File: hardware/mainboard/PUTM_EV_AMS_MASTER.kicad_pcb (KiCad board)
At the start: 4 copper layers, 60 x 100 mm, 207 parts, among them IC1 3.3V/0.5A, IC2 TPS54202HDDCR, IC3 BQ79600PWRQ1, IC6 AMC3330DWER, IC7 AMC3330DWER, IC8 ADC 24bit, IC9 LTC1799, J1 M80-5100642, J10 M300-MV10345M1, J2 M80-5102042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

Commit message: chore: sync
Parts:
- removed C34, C44, C83, C84, C85: 100nF, Capacitor_SMD:C_0603_1608Metric
- removed D10, D13, D18, D19, D24, D8, D9: 60V/0.5/3A, Diode_SMD:D_SOD-123
- removed Q1, Q2, Q3, Q7: DMT6018LDR-7, Samacsys:DMT6018LDR7
- removed R30, R37, R44, R45, R5, R58, R59: 100, Resistor_SMD:R_0603_1608Metric
- removed R46, R47, R48, R56, R57, R60, R61, R71: 10k, Resistor_SMD:R_0603_1608Metric
- removed U2: FT230XS, Package_SO:SSOP-16_3.9x4.9mm_P0.635mm
- added C1: 22uF, Capacitor_SMD:C_0805_2012Metric, F.Cu at (51.5, 154.5)
- J1: value M80-5100642 -> Conn_02x10_Odd_Even; footprint Samacsys:M80-51006YY -> Connector_PinHeader_2.00mm:PinHeader_2x10_P2.00mm_Vertical
- J2: value M80-5102042 -> Conn_02x03_Odd_Even; footprint Samacsys:M80-51020YY -> Connector_PinHeader_2.00mm:PinHeader_2x03_P2.00mm_Vertical
- J3: value M80-5100842 -> Conn_02x04_Odd_Even; footprint Samacsys:M80-51008YY -> Connector_PinHeader_2.00mm:PinHeader_2x04_P2.00mm_Vertical
- moved D16 75.6 mm to (74.4, 144.2)
- moved D5 75.6 mm to (74.4, 144.2)
- moved C11 75.6 mm to (56.2, 142.1)
- moved C12 75.6 mm to (59.7, 140.1)
- moved C13 75.6 mm to (44.9, 130.6)
- moved C14 75.6 mm to (44.9, 129.1)
- moved C17 75.6 mm to (59.7, 138.1)
- moved C19 75.6 mm to (69.4, 97.6)
- moved C20 75.6 mm to (69.4, 95.6)
- moved C21 75.6 mm to (59.7, 142.1)
- moved C22 75.6 mm to (56.2, 138.1)
- moved C23 75.6 mm to (51.9, 118.1)
- moved C24 75.6 mm to (63.4, 111.1)
- moved C25 75.6 mm to (61.2, 120.4)
- moved C26 75.6 mm to (56.2, 140.1)
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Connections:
- net Net-(IC8-CH0+) renamed /ADC/+5VA_MEAS
- D11 pad 1: /EX_CANFD2_TX -> /CTX2
- D11 pad 2: /EX_CANFD2_RX -> /CRX2
- D12 pad 1: /D+ -> /UTX
- D12 pad 2: /D- -> /URX
- D4 pad 1: /EX_CANFD1_TX -> /CTX1
- D4 pad 2: /EX_CANFD1_RX -> /CRX1
- J1 pad 1: /AIR_M- -> /D-
- J1 pad 2: /AIR_P- -> GND
- J1 pad 3: /AIR_PRE- -> /D+
- J1 pad 4: +24V -> VBUS+
- J1 pad 5: +24V -> /EX_CANFD1_RX
- J1 pad 6: +24V -> /CHARGER_DETECTION
- J2 pad 1: /D- -> /AIR_M-
- J2 pad 2: /D+ -> unconnected-(J2-Pin_2-Pad2)
- J2 pad 3: /EX_CANFD1_RX -> /AIR_P-
- J2 pad 4: /EX_CANFD1_TX -> unconnected-(J2-Pin_4-Pad4)
- J2 pad 5: /EX_CANFD2_RX -> /AIR_PRE-
- J2 pad 6: /EX_CANFD2_TX -> unconnected-(J2-Pin_6-Pad6)
- J3 pad 2: /FAN2- -> unconnected-(J3-Pin_2-Pad2)
- J3 pad 3: /FAN3- -> /FAN2-
- J3 pad 4: /FAN4- -> unconnected-(J3-Pin_4-Pad4)
- J3 pad 5: +24V -> /FAN3-
- J3 pad 6: +24V -> unconnected-(J3-Pin_6-Pad6)
- J3 pad 7: +24V -> /FAN4-
- J3 pad 8: +24V -> unconnected-(J3-Pin_8-Pad8)
- R7 pad 1: /D+ -> /Connectivity/EX_FTDI_D+
- R7 pad 2: /Connectivity/FTDIU+ -> /UTX
- R8 pad 1: /Connectivity/FTDIU- -> /URX
- R8 pad 2: /D- -> /Connectivity/EX_FTDI_D-
- U10 pad 2: /Connectivity/~{FTDI_RST} -> /MCU/~{FTDI_RST}
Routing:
- net GND: track 144.5 -> 13.5 mm, vias 103 -> 7
- net (no net): track 88.8 -> 0.00 mm
- net +24V: track 74.5 -> 0.00 mm, vias 7 -> 0
- net VBUS+: track 67.7 -> 0.00 mm, vias 2 -> 0
- net /AIR_PRE_DETECTION: track 63.7 -> 0.00 mm, vias 3 -> 0
- net /AIR_P_DETECTION: track 59.5 -> 0.00 mm, vias 3 -> 0
- net /AIR_M_DETECTION: track 58.8 -> 0.00 mm, vias 1 -> 0
- net /CHARGER_DETECTION: track 56.3 -> 0.00 mm, vias 1 -> 0
- net /SWCLK: track 56.0 -> 0.00 mm, vias 2 -> 0
- net /SWDIO: track 48.3 -> 0.00 mm, vias 2 -> 0
- net /AMS_ERROR: track 46.3 -> 0.00 mm, vias 3 -> 0
- net /UART_TX: track 45.7 -> 0.00 mm, vias 2 -> 0
- net /DETVUSB: track 44.7 -> 0.00 mm, vias 2 -> 0
- net /FC1: track 44.1 -> 0.00 mm, vias 1 -> 0
- net /UART_RX: track 42.7 -> 0.00 mm, vias 2 -> 0
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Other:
- board text removed: "IN"
- board text removed: "OUT"

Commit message: jenrzej colab
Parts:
- moved J8 5.70 mm to (158.5, 83.3)
- moved J4 3.57 mm to (105.5, 91.4)
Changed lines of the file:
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@@
 	(footprint "Samacsys:FTSH-107-XX-YYY-D-K"
 		(layer "F.Cu")
-		(at 105.5 95 90)
+		(at 105.5 91.43 90)
 		(descr "FTSH-107-XX-YYY-D-K")
 		(tags "Connector")
@@
 	(footprint "Samacsys:M80-51004YY"
 		(layer "F.Cu")
-		(at 158.5 89 -90)
+		(at 158.5 83.3 -90)
 		(descr "M80-51004YY")
 		(tags "Connector")

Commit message: Cleaned up schematic, changed USB to UART, changed pinout of AIR sandwich connector
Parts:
- removed C1, C11, C12, C17, C26, C68: 22uF, Capacitor_SMD:C_0805_2012Metric
- removed C13, C14, C3: 1uF, Capacitor_SMD:C_0603_1608Metric
- removed C19, C20, C4, C5: 2.2uF, Capacitor_SMD:C_0603_1608Metric
- removed C21, C22, C39, C40, C42, C56, C57: 100nF, Capacitor_SMD:C_0603_1608Metric
- removed C27, C6, C65: 22uF, Capacitor_SMD:CP_Elec_4x5.8
- removed D12: 5.3V/400W, Package_TO_SOT_SMD:SOT-23-3
- removed D14: 6V, Diode_SMD:D_SOD-123
- removed D16: 30V, Diode_SMD:D_SOD-123
- removed F2: 5A/24V, Fuse:Fuse_2920_7451Metric
- removed F4, F5, F8: 5V/0.5A, Fuse:Fuse_0805_2012Metric
- removed FB1, FB2: 100@100Mhz, Inductor_SMD:L_0603_1608Metric
- removed the H3 at (158.5, 144.5)
- removed IC1: 3.3V/0.5A, Package_TO_SOT_SMD:SOT-23-5
- removed IC2: TPS54202HDDCR, Package_TO_SOT_SMD:SOT-23-6
- removed L4: 68uF/1.4A, Inductor_SMD:L_TDK_VLS6045EX_VLS6045AF
- removed Q4: SI2347DS-T1-GE3, Package_TO_SOT_SMD:SOT-23-3
- removed R10: 100k, Resistor_SMD:R_0603_1608Metric_Pad0.98x0.95mm_HandSolder
- removed R16: 20k, Resistor_SMD:R_0603_1608Metric
- removed R23: 510k, Resistor_SMD:R_0603_1608Metric
- removed R28, R35, R39: 100k, Resistor_SMD:R_0603_1608Metric
- removed R29: 13.3k, Resistor_SMD:R_0603_1608Metric
- removed R32: 10k, Resistor_SMD:R_0603_1608Metric
- removed R40: 400, Resistor_SMD:R_0603_1608Metric
- removed R7, R8: 27, Resistor_SMD:R_0603_1608Metric
- removed TP3, TP9: TestPoint_Small, TestPoint:TestPoint_THTPad_D1.0mm_Drill0.5mm
- removed U4: TPS2113PWR, Package_SO:TSSOP-8_4.4x3mm_P0.65mm
- added H1: M3, MountingHole:MountingHole_3.2mm_M3, F.Cu at (158.5, 86.5)
- D5: value 10V -> ESDS304; footprint Diode_SMD:D_SOD-123 -> Package_TO_SOT_SMD:SOT-23-5_HandSoldering
- moved R73 123.4 mm to (66.4, 92.5)
- moved C96 123.1 mm to (66.4, 91.0)
- moved R72 120.3 mm to (69.3, 91.0)
- moved D5 111.4 mm to (182.6, 117.5)
- moved C23 85.8 mm to (137.6, 121.3)
- moved C29 83.3 mm to (135.6, 132.4), turned to 180 degrees
- moved C28 83.3 mm to (134.7, 121.3)
- moved C36 78.5 mm to (135.4, 124.5), turned to -90 degrees
- moved C70 78.2 mm to (137.4, 124.5), turned to -90 degrees
- moved U10 76.9 mm to (133.6, 126.7), turned to 90 degrees
- moved C25 75.0 mm to (136.1, 121.3), turned to 90 degrees
- moved C86 73.9 mm to (127.9, 112.6), turned to 180 degrees
- moved C24 71.5 mm to (133.7, 124.3)
- moved D27 70.9 mm to (110.1, 134.5)
- moved C87 70.9 mm to (130.3, 130.0), turned to 0 degrees
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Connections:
- D5 pad 1: +24V -> /UART_RX
- D5 pad 2: Net-(D5-A) -> GND
- J1 pad 1: /D- -> /UART_TX
- J1 pad 10: /AIR_PRE_DETECTION -> unconnected-(J1-Pin_10-Pad10)
- J1 pad 12: /AIR_M_DETECTION -> unconnected-(J1-Pin_12-Pad12)
- J1 pad 15: unconnected-(J1-Pin_15-Pad15) -> +5VA
- J1 pad 19: VDD -> +3.3VA
- J1 pad 3: /D+ -> /UART_RX
- J1 pad 4: VBUS+ -> /DETVUSB
- J1 pad 6: /CHARGER_DETECTION -> /UART_RST
- J1 pad 8: /AIR_P_DETECTION -> unconnected-(J1-Pin_8-Pad8)
- U10 pad 14: /FC1 -> /FAN1-
- U10 pad 15: /FC2 -> /FAN2-
- U10 pad 16: /FC3 -> /FAN3-
- U10 pad 17: /FC4 -> /FAN4-
- U10 pad 2: /MCU/~{FTDI_RST} -> /UART_RST
- U10 pad 33: /SAE -> /AIR_PRE-
- U10 pad 34: /SAP -> /AIR_P-
- U10 pad 35: /SAM -> /AIR_M-
- U10 pad 42: /UTX -> /UART_RX
- U10 pad 43: /URX -> /UART_TX
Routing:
- net /ADC/ACU_V-: track 12.6 -> 0.00 mm
- net /Safety/LATCHERR: track 0.00 -> 9.71 mm, vias 0 -> 1
- net +5VIO: track 9.08 -> 18.5 mm, vias 2 -> 4
- net /CRX2: track 0.00 -> 8.41 mm
- net Net-(R14-Pad2): track 0.00 -> 7.63 mm, vias 0 -> 1
- net /CTX2: track 0.00 -> 7.51 mm
- net /Safety/CT_G: track 0.00 -> 7.37 mm, vias 0 -> 1
- net /CRX1: track 0.00 -> 7.06 mm
- net /CTX1: track 0.00 -> 7.02 mm
- net /AMS_ERROR: track 0.00 -> 4.94 mm, vias 0 -> 1
- net /Safety/CAP_VOLT: track 0.00 -> 4.28 mm, vias 0 -> 1
- net /CAR_I: track 0.00 -> 4.20 mm
- net /Isolated SPI/OUT+: track 3.75 -> 0.00 mm
- net /Isolated SPI/OUT-: track 3.71 -> 0.00 mm
- net /ADC/+5VA_MEAS: track 0.00 -> 2.87 mm
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- added copper zone on B.Cu, net GND
- added copper zone on F.Cu, net GND
- added copper zone on In2.Cu, net GND
- removed copper zone on In2.Cu, net +24V
- removed copper zone on In2.Cu, net +3.3VA
- removed copper zone on In2.Cu, net +3.3VIO
- removed copper zone on In2.Cu, net +3.3VMCU
- removed copper zone on In2.Cu, net +5VA
- removed copper zone on In2.Cu, net +5VIO
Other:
- board text added: "UART"
- board text removed: "24V"
- board text removed: "3.3V"
- board text removed: "5V"
- board text removed: "AIR CR"
- board text removed: "ANALOG PWR"
- board text removed: "FAN CR"
- board text removed: "LEDS"
- board text removed: "MUX5V"
- board text removed: "USB"
- board text removed: "USB5V"

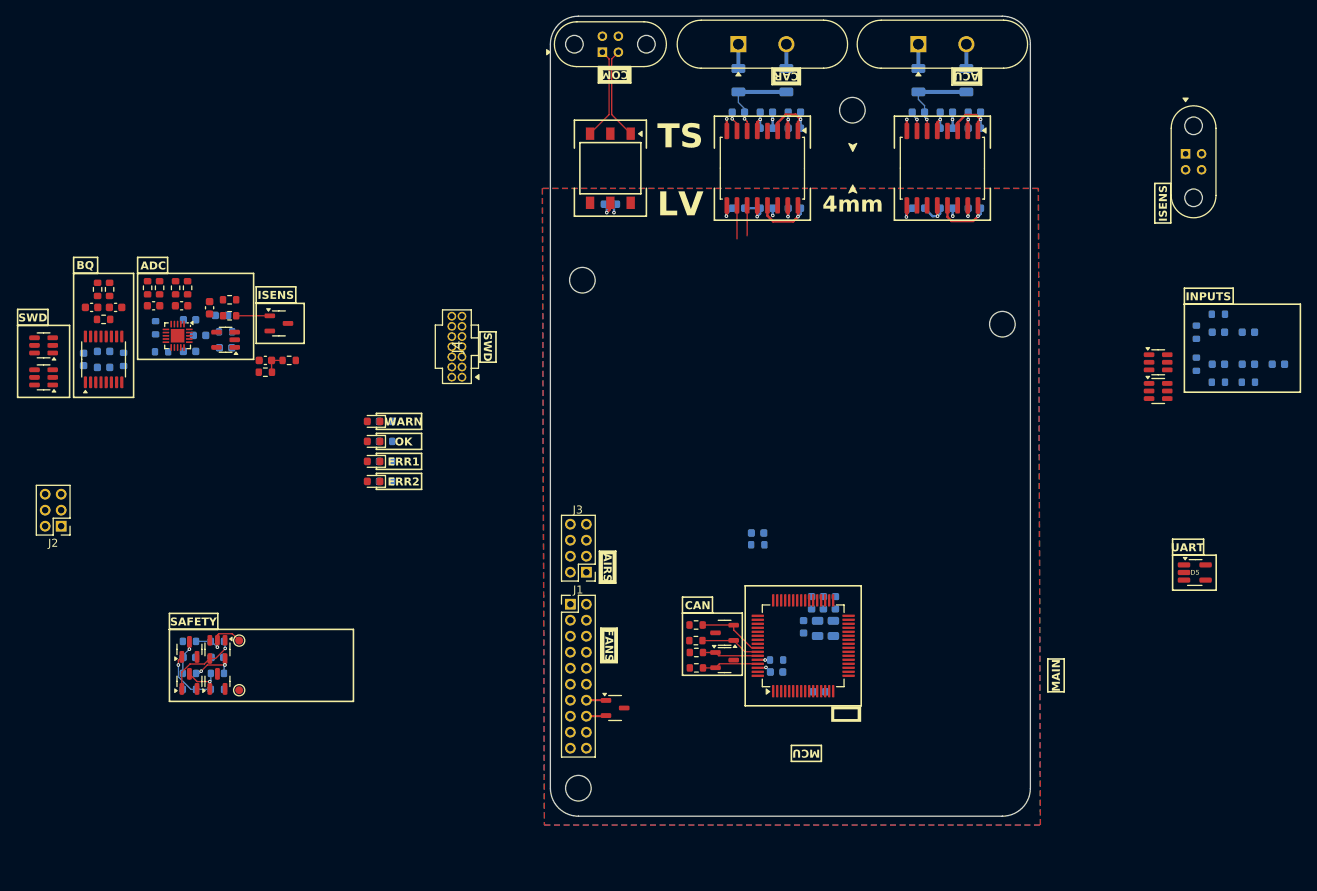
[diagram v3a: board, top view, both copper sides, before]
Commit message: Routed AIR detection signal to main connector
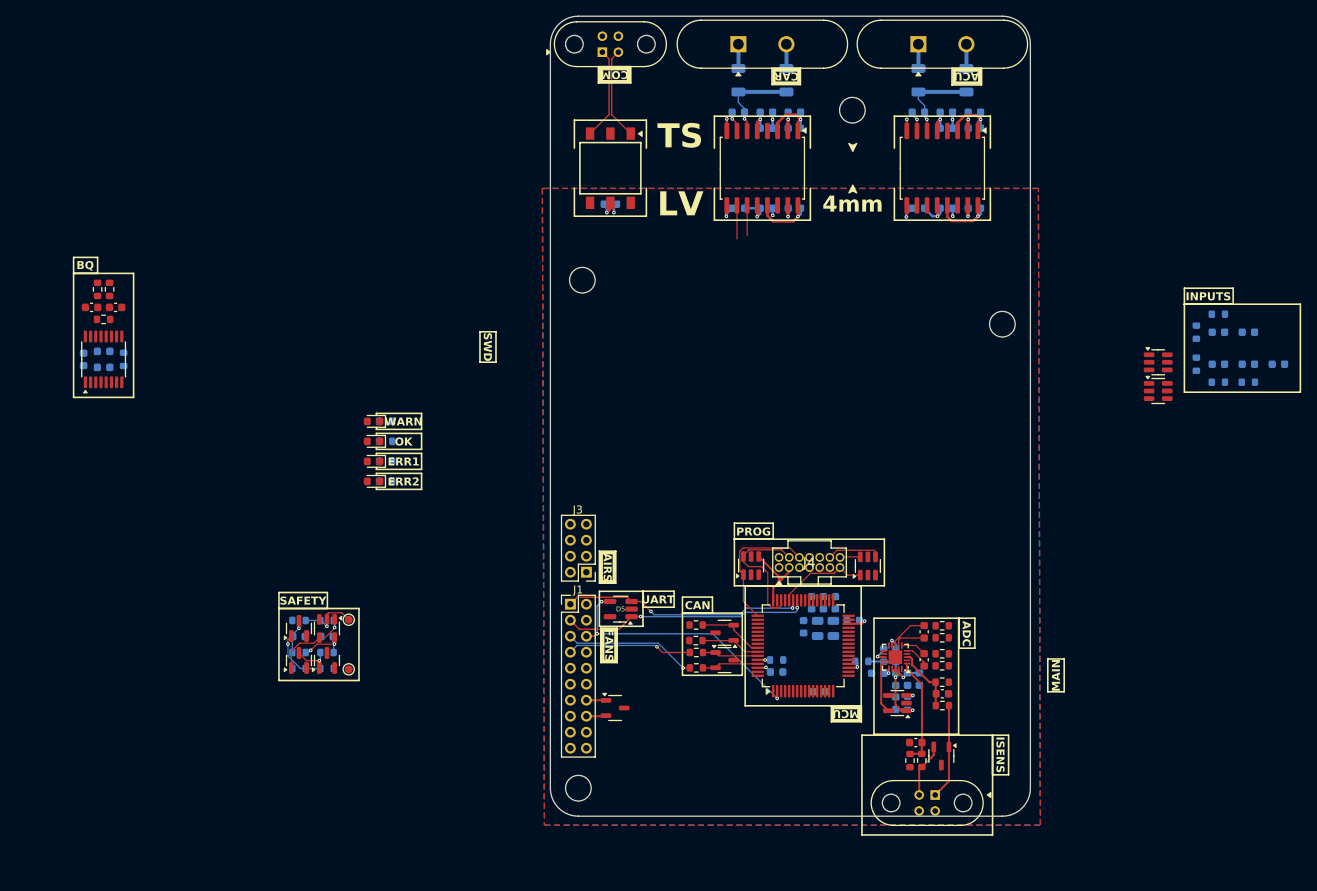
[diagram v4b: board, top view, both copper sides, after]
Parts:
- removed J2: Conn_02x03_Odd_Even, Connector_PinHeader_2.00mm:PinHeader_2x03_P2.00mm_Vertical
- moved R54 107.9 mm to (151.0, 124.2), turned to 180 degrees
- moved R52 107.2 mm to (151.0, 125.7), turned to 0 degrees
- moved D21 106.7 mm to (141.7, 116.7), turned to 90 degrees
- moved R51 106.2 mm to (151.0, 127.7), turned to 180 degrees
- moved R50 105.5 mm to (151.0, 129.2), turned to 0 degrees
- moved C90 104.6 mm to (148.7, 124.9), turned to -90 degrees
- moved C88 103.5 mm to (151.0, 132.7), turned to 180 degrees
- moved C89 102.8 mm to (148.7, 128.4), turned to -90 degrees
- moved R33 101.5 mm to (151.0, 134.2)
- moved R22 101.2 mm to (145.2, 127.9), turned to -90 degrees
- moved R43 101.1 mm to (151.0, 131.2)
- moved C45 100.4 mm to (146.6, 130.9), turned to -90 degrees
- moved D23 98.9 mm to (150.9, 140.5), turned to -90 degrees
- moved C46 98.4 mm to (148.1, 130.9), turned to -90 degrees
- moved IC8 98.3 mm to (145.1, 128.1), turned to 180 degrees
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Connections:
- D21 pad 1: /UART_RX -> /UART_DBG_RX
- D21 pad 6: /UART_TX -> /UART_DBG_TX
- D22 pad 4: +3.3VIO -> +3.3VMCU
- J3 pad 2: unconnected-(J3-Pin_2-Pad2) -> /AIR_PRE-
- J3 pad 4: unconnected-(J3-Pin_4-Pad4) -> /AIR_P-
- J3 pad 6: unconnected-(J3-Pin_6-Pad6) -> /AIR_M-
- J3 pad 8: unconnected-(J3-Pin_8-Pad8) -> GND
- J4 pad 13: /UART_RX -> /UART_DBG_RX
- J4 pad 14: /UART_TX -> /UART_DBG_TX
- J4 pad 3: +3.3VIO -> +3.3VMCU
- J8 pad 1: +5VA -> /CAR_I
- J8 pad 2: /CAR_I -> +5VA
- U10 pad 15: /FAN2- -> /MCU/FAN2_CTRL
- U10 pad 16: /FAN3- -> /MCU/FAN3_CTRL
- U10 pad 17: /FAN4- -> /MCU/FAN4_CTRL
- U10 pad 33: /AIR_PRE- -> /MCU/SIGNAL_AIR_PRE
- U10 pad 44: /UART_RX -> /UART_DBG_RX
- U10 pad 45: /UART_TX -> /UART_DBG_TX
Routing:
- net /UART_RST: track 0.00 -> 33.5 mm, vias 0 -> 3
- net /UART_RX: track 0.00 -> 31.1 mm, vias 0 -> 2
- net /UART_TX: track 0.00 -> 30.4 mm, vias 0 -> 2
- net /SWDIO: track 0.00 -> 17.3 mm
- net /SWCLK: track 0.00 -> 17.1 mm
- net /EX_CANFD1_RX: track 0.00 -> 16.6 mm, vias 0 -> 1
- net /EX_CANFD1_TX: track 0.00 -> 15.6 mm, vias 0 -> 1
- net +3.3VIO: track 2.46 -> 17.1 mm, vias 0 -> 2
- net /UART_DBG_RX: track 0.00 -> 11.4 mm
- net +3.3VMCU: track 0.00 -> 10.9 mm, vias 0 -> 1
- net /ADC/+5VA_MEAS: track 2.87 -> 13.5 mm
- net /ADC/I+: track 0.00 -> 8.22 mm
- net /CAR_I: track 4.20 -> 12.1 mm
- net /NRST: track 0.00 -> 6.80 mm
- net +5VA: track 0.00 -> 6.77 mm
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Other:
- board text added: "PROG"

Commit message: First board revision
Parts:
- added H1: MountingHole_Pad, MountingHole:MountingHole_3.2mm_M3_Pad_Via, F.Cu at (158.5, 144.5)
- moved R21 81.2 mm to (127.2, 141.8), turned to -90 degrees
- moved C103 81.0 mm to (125.8, 141.8), turned to 90 degrees
- moved C104 80.2 mm to (130.2, 141.8), turned to 90 degrees
- moved C105 79.4 mm to (128.9, 138.3), turned to -90 degrees
- moved R25 77.3 mm to (128.7, 141.8), turned to -90 degrees
- moved R26 75.1 mm to (127.5, 138.3)
- moved C101 73.3 mm to (132.2, 141.8), turned to 90 degrees
- moved C102 73.1 mm to (136.6, 141.8), turned to 90 degrees
- moved R17 70.3 mm to (133.7, 141.8), turned to -90 degrees
- moved D25 69.9 mm to (128.0, 140.1), turned to 90 degrees
- moved R20 69.6 mm to (135.1, 141.8), turned to -90 degrees
- moved C43 68.1 mm to (114.0, 83.8)
- moved C53 68.1 mm to (111.5, 84.8)
- moved C78 68.1 mm to (114.0, 85.8)
- moved C79 68.1 mm to (112.5, 78.2)
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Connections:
- J1 pad 10: unconnected-(J1-Pin_10-Pad10) -> /AIR_M_DETECTION
- J1 pad 12: unconnected-(J1-Pin_12-Pad12) -> /AIR_P_DETECTION
- J1 pad 18: unconnected-(J1-Pin_18-Pad18) -> /CHARGER_DETECTION
- J1 pad 8: unconnected-(J1-Pin_8-Pad8) -> /AIR_PRE_DETECTION
- U10 pad 15: /MCU/FAN2_CTRL -> /FAN2-
- U10 pad 16: /MCU/FAN3_CTRL -> /FAN3-
- U10 pad 17: /MCU/FAN4_CTRL -> /FAN4-
- U10 pad 33: /MCU/SIGNAL_AIR_PRE -> /AIR_PRE-
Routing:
- net +5VIO: track 18.5 -> 145.9 mm, vias 4 -> 6
- net +3.3VIO: track 17.1 -> 126.7 mm, vias 2 -> 6
- net +5VA: track 6.77 -> 74.9 mm, vias 0 -> 1
- net /ADC/CAR_V+: track 3.79 -> 66.3 mm
- net /ADC/CAR_V-: track 4.17 -> 64.8 mm
- net /ADC/ACU_V+: track 0.00 -> 59.6 mm
- net /ADC/ACU_V-: track 0.00 -> 58.5 mm
- net /UCRX: track 0.00 -> 57.6 mm, vias 0 -> 2
- net /UCTX: track 0.00 -> 55.8 mm
- net /~{FLT}: track 0.00 -> 54.6 mm, vias 0 -> 3
- net +3.3VA: track 3.55 -> 48.8 mm
- net /DETVUSB: track 0.00 -> 42.3 mm, vias 0 -> 1
- net /FAN4-: track 0.00 -> 40.6 mm, vias 0 -> 1
- net /FAN3-: track 0.00 -> 39.6 mm, vias 0 -> 1
- net /TSMS_DETECTION: track 0.00 -> 38.5 mm
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- added copper zone on B.Cu, net +3.3VMCU
- added copper zone on F.Cu, net +3.3VMCU
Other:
- board text removed: "SWD"
